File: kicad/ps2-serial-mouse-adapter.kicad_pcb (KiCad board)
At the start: 2 copper layers, 68.9 x 34 mm, 8 parts, among them U1 Arduino_Nano, U2 MAX3232_HW027

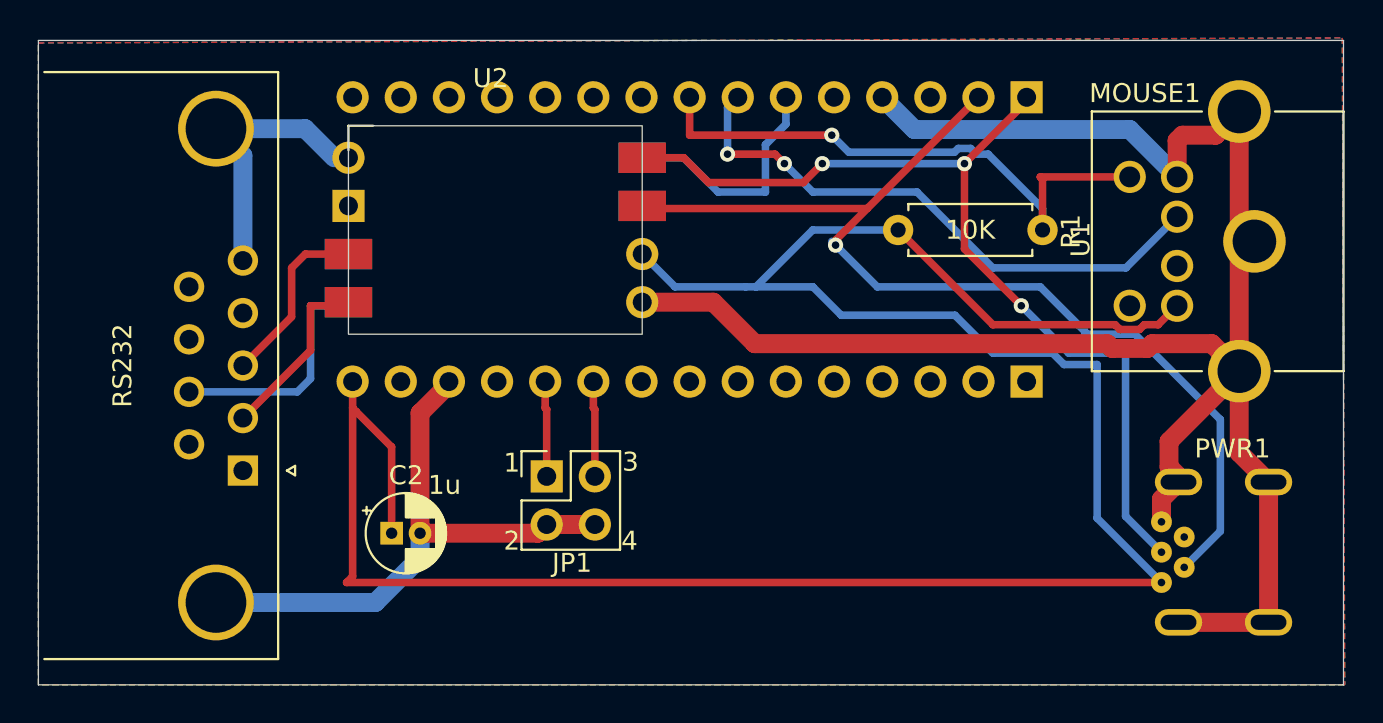
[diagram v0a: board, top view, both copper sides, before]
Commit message: Improve trace routing for better printing and fix net assignments
- Rerouted traces for cleaner print output
- Fixed VBUS and jumper net assignments (were incorrectly marked unconnected)
- Expand .gitignore to exclude KiCad autosave, lock, cache, history, and .kicad_prl
- Untrack .kicad_prl (machine-specific local preferences)

Co-Authored-By: Claude Sonnet 4.6 <noreply@anthropic.com>
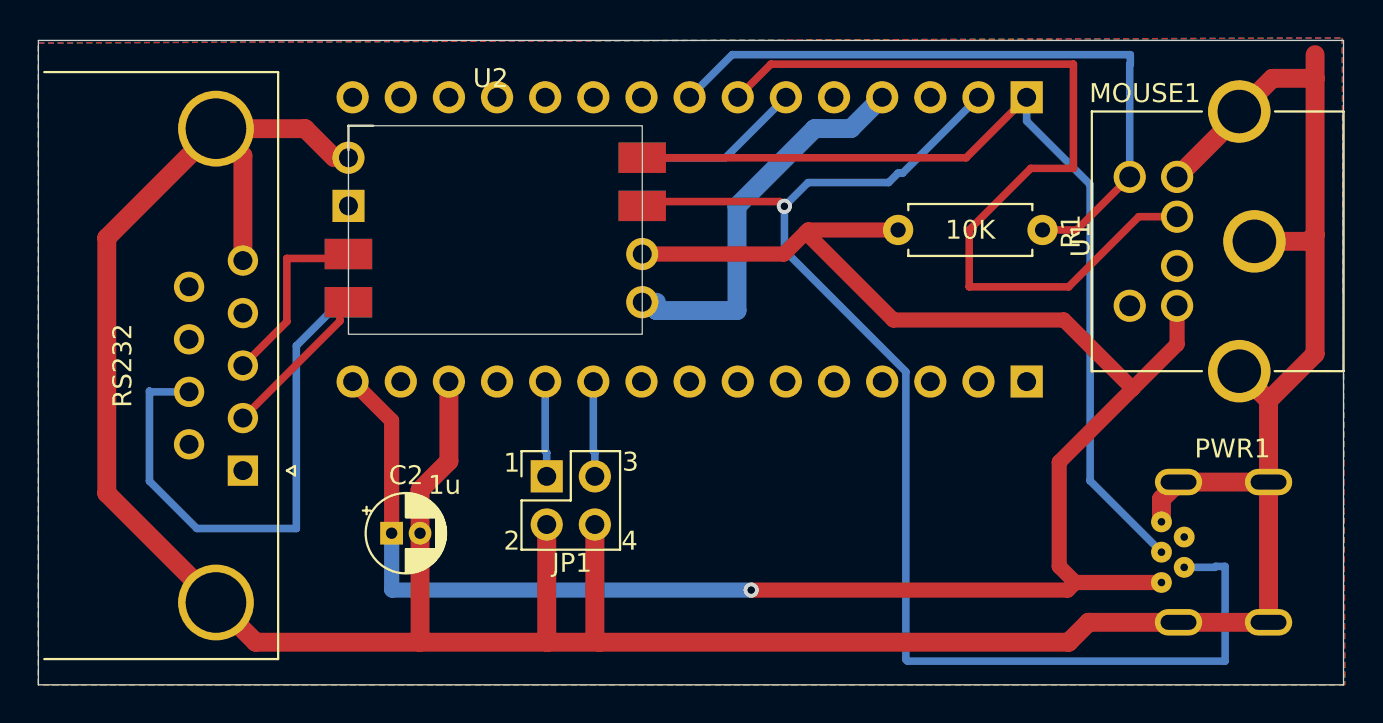
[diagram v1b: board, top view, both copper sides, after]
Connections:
- C2 pad 1: unconnected-(C2-Pad1) -> VBUS
- JP1 pad 1: unconnected-(C2-Pad1) -> Net-(JP1-Pin_1)
- JP1 pad 3: unconnected-(C2-Pad1) -> Net-(JP1-Pin_3)
- MOUSE1 pad 4: unconnected-(C2-Pad1) -> VBUS
- PWR1 pad 1: unconnected-(C2-Pad1) -> VBUS
- R1 pad 1: unconnected-(C2-Pad1) -> VBUS
- U1 pad 16: unconnected-(C2-Pad1) -> unconnected-(U1-D13-Pad16)
- U1 pad 17: unconnected-(C2-Pad1) -> unconnected-(U1-3V3-Pad17)
- U1 pad 18: unconnected-(C2-Pad1) -> unconnected-(U1-AREF-Pad18)
- U1 pad 19: unconnected-(C2-Pad1) -> unconnected-(U1-A0-Pad19)
- U1 pad 20: unconnected-(C2-Pad1) -> unconnected-(U1-A1-Pad20)
- U1 pad 21: unconnected-(C2-Pad1) -> unconnected-(U1-A2-Pad21)
- U1 pad 22: unconnected-(C2-Pad1) -> unconnected-(U1-A3-Pad22)
- U1 pad 23: unconnected-(C2-Pad1) -> unconnected-(U1-A4-Pad23)
- U1 pad 24: unconnected-(C2-Pad1) -> unconnected-(U1-A5-Pad24)
- U1 pad 25: unconnected-(C2-Pad1) -> Net-(JP1-Pin_3)
- U1 pad 26: unconnected-(C2-Pad1) -> Net-(JP1-Pin_1)
- U1 pad 30: unconnected-(C2-Pad1) -> VBUS
- U2 pad 1: unconnected-(C2-Pad1) -> VBUS
- U2 pad 3: unconnected-(C2-Pad1) -> VBUS
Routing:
- net unconnected-(C2-Pad1): track 137.2 -> 0.00 mm
- net VBUS: track 0.00 -> 104.4 mm, vias 0 -> 1
- net GND: track 145.8 -> 204.0 mm
- net Net-(U2-RS232_RXD2): track 12.3 -> 28.5 mm
- net DATA: track 31.2 -> 46.3 mm, vias 2 -> 0
- net RX: track 55.6 -> 70.6 mm
- net CLK: track 31.1 -> 36.4 mm, vias 1 -> 0
- net Net-(JP1-Pin_3): track 0.00 -> 5.03 mm
- net Net-(JP1-Pin_1): track 0.00 -> 5.03 mm
- net RTS: track 12.2 -> 8.45 mm
- net Net-(U2-RS232_TXD1): track 9.39 -> 8.24 mm
- net TX: track 48.7 -> 48.1 mm, vias 3 -> 0
- net Net-(U2-RS232_RXD1): track 9.49 -> 10.1 mm
